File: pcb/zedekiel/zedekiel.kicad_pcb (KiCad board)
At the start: 2 copper layers, 150 parts, among them J2 USB_C_Receptacle_USB2.0, K1 KEYSW, K10 KEYSW, K11 KEYSW, K12 KEYSW, K13 KEYSW, K14 KEYSW, K15 KEYSW, K16 KEYSW, K17 KEYSW, K18 KEYSW, K19 KEYSW, K2 KEYSW, K20 KEYSW, K21 KEYSW, K22 KEYSW, K23 KEYSW, K24 KEYSW, K25 KEYSW, K26 KEYSW, K27 KEYSW, K28 KEYSW, K29 KEYSW, K3 KEYSW, K30 KEYSW, K31 KEYSW, K32 KEYSW, K33 KEYSW, K34 KEYSW, K35 KEYSW, K36 KEYSW, K37 KEYSW, K38 KEYSW, K39 KEYSW, K4 KEYSW, K40 KEYSW, K41 KEYSW, K42 KEYSW, K43 KEYSW, K44 KEYSW, K45 KEYSW, K46 KEYSW, K47 KEYSW, K48 KEYSW, K49 KEYSW, K5 KEYSW, K50 KEYSW, K51 KEYSW, K52 KEYSW, K53 KEYSW, K54 KEYSW, K55 KEYSW, K56 KEYSW, K57 KEYSW, K58 KEYSW, K59 KEYSW, K6 KEYSW, K60 KEYSW, K61 KEYSW, K62 KEYSW, K63 KEYSW, K64 KEYSW, K65 KEYSW, K66 KEYSW, K7 KEYSW, K8 KEYSW, K9 KEYSW, SW1 SW_PUSH, U1 ATmega16U4-AU_(modified), X1 16MHz

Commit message: Diodes and sockets in place
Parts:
- C1, C2, C3, C4, C5, C6, C7, C8, D1, D10, D11, D12, D13, D14, D15, D16, D17, D18, D19, D2, D20, D21, D22, D23, D24, D25, D26, D27, D28, D29, D3, D30, D31, D32, D33, D34, D35, D36, D37, D38, D39, D4, D40, D41, D42, D43, D44, D45, D46, D47, D48, D49, D5, D50, D51, D52, D53, D54, D55, D56, D57, D58, D59, D6, D60, D61, D62, D63, D64, D65, D66, D7, D8, D9, R1, R2, R3, R4, R5, R6, SW1, X1: moved to B.Cu
- moved D56 279.8 mm to (318.2, 92.8), turned to 270 degrees
- moved D55 246.5 mm to (285.0, 92.8), turned to 270 degrees
- moved D54 238.5 mm to (256.4, 92.8), turned to 270 degrees
- moved D42 236.8 mm to (313.4, 73.8), turned to 270 degrees
- moved D64 234.8 mm to (265.8, 111.8), turned to 270 degrees
- moved D63 234.0 mm to (235.0, 111.8), turned to 270 degrees
- moved D65 212.7 mm to (296.6, 111.8), turned to 270 degrees
- moved D41 206.5 mm to (285.0, 73.8), turned to 270 degrees
- moved D66 206.1 mm to (318.2, 35.8), turned to 270 degrees
- moved D62 205.4 mm to (211.2, 111.8), turned to 270 degrees
- moved D53 202.8 mm to (237.4, 92.8), turned to 270 degrees
- moved D61 185.3 mm to (187.4, 111.8), turned to 270 degrees
- moved D52 183.0 mm to (218.4, 92.8), turned to 270 degrees
- moved D40 171.7 mm to (266.0, 73.8), turned to 270 degrees
- moved D39 170.0 mm to (247.0, 73.8), turned to 270 degrees
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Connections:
- K1 pad 1: Net-(D1-Pad1) -> /R1
- K1 pad 2: /R1 -> Net-(D1-Pad1)
- K10 pad 1: Net-(D10-Pad1) -> /R1
- K10 pad 2: /R1 -> Net-(D10-Pad1)
- K11 pad 1: Net-(D11-Pad1) -> /R1
- K11 pad 2: /R1 -> Net-(D11-Pad1)
- K12 pad 1: Net-(D12-Pad1) -> /R1
- K12 pad 2: /R1 -> Net-(D12-Pad1)
- K13 pad 1: Net-(D13-Pad1) -> /R1
- K13 pad 2: /R1 -> Net-(D13-Pad1)
- K14 pad 1: Net-(D14-Pad1) -> /R1
- K14 pad 2: /R1 -> Net-(D14-Pad1)
- K15 pad 1: Net-(D15-Pad1) -> /R2
- K15 pad 2: /R2 -> Net-(D15-Pad1)
- K16 pad 1: Net-(D16-Pad1) -> /R2
- K16 pad 2: /R2 -> Net-(D16-Pad1)
- K17 pad 1: Net-(D17-Pad1) -> /R2
- K17 pad 2: /R2 -> Net-(D17-Pad1)
- K18 pad 1: Net-(D18-Pad1) -> /R2
- K18 pad 2: /R2 -> Net-(D18-Pad1)
- K19 pad 1: Net-(D19-Pad1) -> /R2
- K19 pad 2: /R2 -> Net-(D19-Pad1)
- K2 pad 1: Net-(D2-Pad1) -> /R1
- K2 pad 2: /R1 -> Net-(D2-Pad1)
- K20 pad 1: Net-(D20-Pad1) -> /R2
- K20 pad 2: /R2 -> Net-(D20-Pad1)
- K21 pad 1: Net-(D21-Pad1) -> /R2
- K21 pad 2: /R2 -> Net-(D21-Pad1)
- K22 pad 1: Net-(D22-Pad1) -> /R2
- K22 pad 2: /R2 -> Net-(D22-Pad1)
- K23 pad 1: Net-(D23-Pad1) -> /R2
- K23 pad 2: /R2 -> Net-(D23-Pad1)
- K24 pad 1: Net-(D24-Pad1) -> /R2
- K24 pad 2: /R2 -> Net-(D24-Pad1)
- K25 pad 1: Net-(D25-Pad1) -> /R2
- K25 pad 2: /R2 -> Net-(D25-Pad1)
- K26 pad 1: Net-(D26-Pad1) -> /R2
- K26 pad 2: /R2 -> Net-(D26-Pad1)
- K27 pad 1: Net-(D27-Pad1) -> /R2
- K27 pad 2: /R2 -> Net-(D27-Pad1)
- K28 pad 1: Net-(D28-Pad1) -> /R2
- K28 pad 2: /R2 -> Net-(D28-Pad1)
- K29 pad 1: Net-(D29-Pad1) -> /R3
- K29 pad 2: /R3 -> Net-(D29-Pad1)
- K3 pad 1: Net-(D3-Pad1) -> /R1
- K3 pad 2: /R1 -> Net-(D3-Pad1)
- K30 pad 1: Net-(D30-Pad1) -> /R3
- K30 pad 2: /R3 -> Net-(D30-Pad1)
- K31 pad 1: Net-(D31-Pad1) -> /R3
- K31 pad 2: /R3 -> Net-(D31-Pad1)
- K32 pad 1: Net-(D32-Pad1) -> /R3
- K32 pad 2: /R3 -> Net-(D32-Pad1)
- K33 pad 1: Net-(D33-Pad1) -> /R3
- K33 pad 2: /R3 -> Net-(D33-Pad1)
- K34 pad 1: Net-(D34-Pad1) -> /R3
- K34 pad 2: /R3 -> Net-(D34-Pad1)
- K35 pad 1: Net-(D35-Pad1) -> /R3
- K35 pad 2: /R3 -> Net-(D35-Pad1)
- K36 pad 1: Net-(D36-Pad1) -> /R3
- K36 pad 2: /R3 -> Net-(D36-Pad1)
- K37 pad 1: Net-(D37-Pad1) -> /R3
- K37 pad 2: /R3 -> Net-(D37-Pad1)
- K38 pad 1: Net-(D38-Pad1) -> /R3
- K38 pad 2: /R3 -> Net-(D38-Pad1)
- K39 pad 1: Net-(D39-Pad1) -> /R3
- K39 pad 2: /R3 -> Net-(D39-Pad1)
- K4 pad 1: Net-(D4-Pad1) -> /R1
- K4 pad 2: /R1 -> Net-(D4-Pad1)
- K40 pad 1: Net-(D40-Pad1) -> /R3
- K40 pad 2: /R3 -> Net-(D40-Pad1)
- K41 pad 1: Net-(D41-Pad1) -> /R3
- K41 pad 2: /R3 -> Net-(D41-Pad1)
- K42 pad 1: Net-(D42-Pad1) -> /R3
- K42 pad 2: /R3 -> Net-(D42-Pad1)
- K43 pad 1: Net-(D43-Pad1) -> /R4
- K43 pad 2: /R4 -> Net-(D43-Pad1)
- K44 pad 1: Net-(D44-Pad1) -> /R4
- K44 pad 2: /R4 -> Net-(D44-Pad1)
- K45 pad 1: Net-(D45-Pad1) -> /R4
- K45 pad 2: /R4 -> Net-(D45-Pad1)
- K46 pad 1: Net-(D46-Pad1) -> /R4
- K46 pad 2: /R4 -> Net-(D46-Pad1)
- K47 pad 1: Net-(D47-Pad1) -> /R4
- K47 pad 2: /R4 -> Net-(D47-Pad1)
- K48 pad 1: Net-(D48-Pad1) -> /R4
- K48 pad 2: /R4 -> Net-(D48-Pad1)
- K49 pad 1: Net-(D49-Pad1) -> /R4
- K49 pad 2: /R4 -> Net-(D49-Pad1)
- K5 pad 1: Net-(D5-Pad1) -> /R1
- K5 pad 2: /R1 -> Net-(D5-Pad1)
- K50 pad 1: Net-(D50-Pad1) -> /R4
- K50 pad 2: /R4 -> Net-(D50-Pad1)
- K51 pad 1: Net-(D51-Pad1) -> /R4
- K51 pad 2: /R4 -> Net-(D51-Pad1)
- K52 pad 1: Net-(D52-Pad1) -> /R4
- K52 pad 2: /R4 -> Net-(D52-Pad1)
- K53 pad 1: Net-(D53-Pad1) -> /R4
- K53 pad 2: /R4 -> Net-(D53-Pad1)
- K54 pad 1: Net-(D54-Pad1) -> /R4
- K54 pad 2: /R4 -> Net-(D54-Pad1)
- K55 pad 1: Net-(D55-Pad1) -> /R4
- K55 pad 2: /R4 -> Net-(D55-Pad1)
- K56 pad 1: Net-(D56-Pad1) -> /R4
- K56 pad 2: /R4 -> Net-(D56-Pad1)
- K57 pad 1: Net-(D57-Pad1) -> /R5
- K57 pad 2: /R5 -> Net-(D57-Pad1)
- K58 pad 1: Net-(D58-Pad1) -> /R5
- K58 pad 2: /R5 -> Net-(D58-Pad1)
- K59 pad 1: Net-(D59-Pad1) -> /R5
- K59 pad 2: /R5 -> Net-(D59-Pad1)
- K6 pad 1: Net-(D6-Pad1) -> /R1
- K6 pad 2: /R1 -> Net-(D6-Pad1)
- K60 pad 1: Net-(D60-Pad1) -> /R5
- K60 pad 2: /R5 -> Net-(D60-Pad1)
- K61 pad 1: Net-(D61-Pad1) -> /R5
- K61 pad 2: /R5 -> Net-(D61-Pad1)
- K62 pad 1: Net-(D62-Pad1) -> /R5
- K62 pad 2: /R5 -> Net-(D62-Pad1)
- K63 pad 1: Net-(D63-Pad1) -> /R5
- K63 pad 2: /R5 -> Net-(D63-Pad1)
- K64 pad 1: Net-(D64-Pad1) -> /R5
- K64 pad 2: /R5 -> Net-(D64-Pad1)
- K65 pad 1: Net-(D65-Pad1) -> /R5
- K65 pad 2: /R5 -> Net-(D65-Pad1)
- K66 pad 1: Net-(D66-Pad1) -> /R5
- K66 pad 2: /R5 -> Net-(D66-Pad1)
- K7 pad 1: Net-(D7-Pad1) -> /R1
- K7 pad 2: /R1 -> Net-(D7-Pad1)
- K8 pad 1: Net-(D8-Pad1) -> /R1
- K8 pad 2: /R1 -> Net-(D8-Pad1)
- K9 pad 1: Net-(D9-Pad1) -> /R1
- K9 pad 2: /R1 -> Net-(D9-Pad1)

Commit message: Holes and stabilizers
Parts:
- added REF**: Stabilizer_MX_2u, custom:Stabilizer_MX_2u, F.Cu at (39.4, 67.9)
- added REF**: Stabilizer_MX_2u, custom:Stabilizer_MX_2u, F.Cu at (303.0, 48.9)
- added REF**: Stabilizer_MX_2u, custom:Stabilizer_MX_2u, F.Cu at (305.4, 67.9)
- added REF**: Stabilizer_MX_2u, custom:Stabilizer_MX_2u, F.Cu at (276.9, 86.9)
- added REF**: Stabilizer_MX_2u, custom:Stabilizer_MX_2u, F.Cu at (257.9, 105.9)
- added REF**: Stabilizer_MX_2u, custom:Stabilizer_MX_2u, F.Cu at (146.3, 105.9)
- added REF**: Stabilizer_MX_2u, custom:Stabilizer_MX_2u, F.Cu at (63.1, 105.9)
- J2, U1: moved to B.Cu
- SW1: moved to F.Cu
- moved R1 235.3 mm to (-24.9, 96.0), turned to 270 degrees
- moved C5 233.5 mm to (-2.05, 80.5)
- moved C6 219.7 mm to (-2.05, 76.4)
- moved C2 219.3 mm to (26.9, 109.1), turned to 180 degrees
- moved R4 218.0 mm to (27.6, 97.7)
- moved R6 213.4 mm to (42.5, 112.9)
- moved C1 211.3 mm to (24.1, 100.9)
- moved C7 201.2 mm to (-2.12, 84.1)
- moved C4 201.1 mm to (-2.15, 72.3)
- moved R5 197.6 mm to (24.4, 97.8)
- moved C8 196.4 mm to (-2.15, 68.3)
- moved C3 192.8 mm to (23.6, 109.1)
- moved R2 190.5 mm to (-7.70, 17.0), turned to 180 degrees
- moved R3 186.2 mm to (-7.54, 12.8), turned to 180 degrees
- moved SW1 125.9 mm to (-26.4, 101.2)
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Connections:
- D57 pad 2: /C1 -> /C2
- D58 pad 2: /C2 -> /C4
- D59 pad 2: /C3 -> /C5
- D60 pad 2: /C4 -> /C7
- D61 pad 2: /C5 -> /C8
- D62 pad 2: /C6 -> /C10
- D63 pad 2: /C7 -> /C11
- D64 pad 2: /C8 -> /C12
- D65 pad 2: /C9 -> /C13
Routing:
- net Net-(D7-Pad1): track 0.00 -> 7.34 mm
- net Net-(D55-Pad1): track 0.00 -> 2.53 mm
- net Net-(D41-Pad1): track 0.00 -> 2.53 mm
- net Net-(D40-Pad1): track 0.00 -> 2.53 mm
- net Net-(D32-Pad1): track 0.00 -> 2.53 mm
- net Net-(D31-Pad1): track 0.00 -> 2.53 mm
- net Net-(D30-Pad1): track 0.00 -> 2.53 mm
- net Net-(D39-Pad1): track 0.00 -> 2.53 mm
- net Net-(D38-Pad1): track 0.00 -> 2.53 mm
- net Net-(D37-Pad1): track 0.00 -> 2.53 mm
- net Net-(D36-Pad1): track 0.00 -> 2.53 mm
- net Net-(D35-Pad1): track 0.00 -> 2.53 mm
- net Net-(D34-Pad1): track 0.00 -> 2.53 mm
- net Net-(D33-Pad1): track 0.00 -> 2.53 mm
- net Net-(D57-Pad1): track 0.00 -> 2.51 mm
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
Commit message: Routing started.
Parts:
- added REF**: hole-indicator, custom:hole-indicator, F.Cu at (297.0, 95.0)
- added REF**: hole-indicator, custom:hole-indicator, F.Cu at (166.4, 105.9)
- added REF**: hole-indicator, custom:hole-indicator, F.Cu at (47.4, 88.8)
- added REF**: hole-indicator, custom:hole-indicator, F.Cu at (248.4, 65.5)
- added REF**: hole-indicator, custom:hole-indicator, F.Cu at (115.4, 65.5)
- added REF**: hole-indicator, custom:hole-indicator, F.Cu at (46.0, 39.4)
- added REF**: hole-indicator, custom:hole-indicator, F.Cu at (298.9, 35.4)
- added REF**: hole-indicator, custom:hole-indicator, F.Cu at (162.9, 38.8)
- moved J2 87.5 mm to (-23.5, 62.6)
- moved R2 87.5 mm to (-77.8, 69.4)
- moved R3 87.5 mm to (-77.6, 65.2)
- moved R5 76.6 mm to (46.0, 24.3), turned to 90 degrees
- moved R4 75.0 mm to (43.1, 24.3), turned to 90 degrees
- moved C5 56.4 mm to (46.4, 109.3), turned to 225 degrees
- moved SW1 50.2 mm to (22.9, 92.0), turned to 270 degrees
- moved R1 47.8 mm to (22.9, 97.9), turned to 90 degrees
- moved C7 47.3 mm to (43.5, 96.5), turned to 315 degrees
- moved C4 42.2 mm to (30.6, 98.9), turned to 45 degrees
- moved C8 41.2 mm to (22.9, 101.0), turned to 270 degrees
- moved C6 40.5 mm to (33.1, 96.4), turned to 45 degrees
- moved R6 12.6 mm to (29.9, 112.9), turned to 180 degrees
- moved C1 6.43 mm to (23.6, 107.3)
- moved C2 0.20 mm to (26.9, 108.9)
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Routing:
- net /R5: track 0.00 -> 336.1 mm, vias 0 -> 10
- net /R4: track 0.00 -> 286.7 mm, vias 0 -> 14
- net /R3: track 0.00 -> 277.2 mm, vias 0 -> 14
- net /R2: track 0.00 -> 276.5 mm, vias 0 -> 14
- net /R1: track 0.00 -> 259.8 mm, vias 0 -> 14
- net /C12: track 0.00 -> 95.1 mm
- net /C7: track 0.00 -> 93.0 mm
- net /C13: track 0.00 -> 92.3 mm
- net /C2: track 0.00 -> 91.2 mm
- net /C8: track 0.00 -> 91.0 mm
- net /C14: track 0.00 -> 89.9 mm
- net /C10: track 0.00 -> 89.7 mm
- net /C5: track 0.00 -> 87.9 mm
- net /C11: track 0.00 -> 87.9 mm
- net /C4: track 0.00 -> 87.7 mm
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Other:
- net class EasyEDA added: clearance 0.2, trace_width 0.254, via_dia 0.61, via_drill 0.305
- board text added: "RESET"

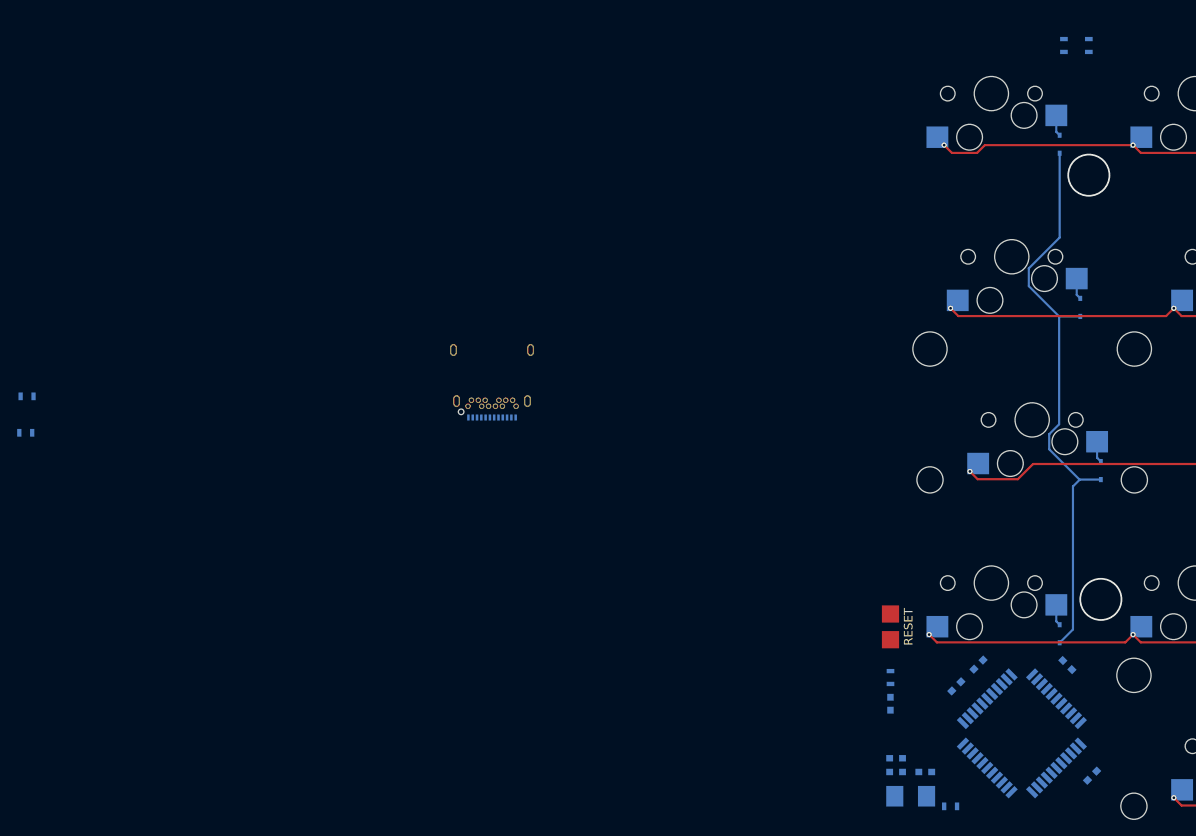
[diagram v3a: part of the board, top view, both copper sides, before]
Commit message: Routing. Fixed a moved socket.
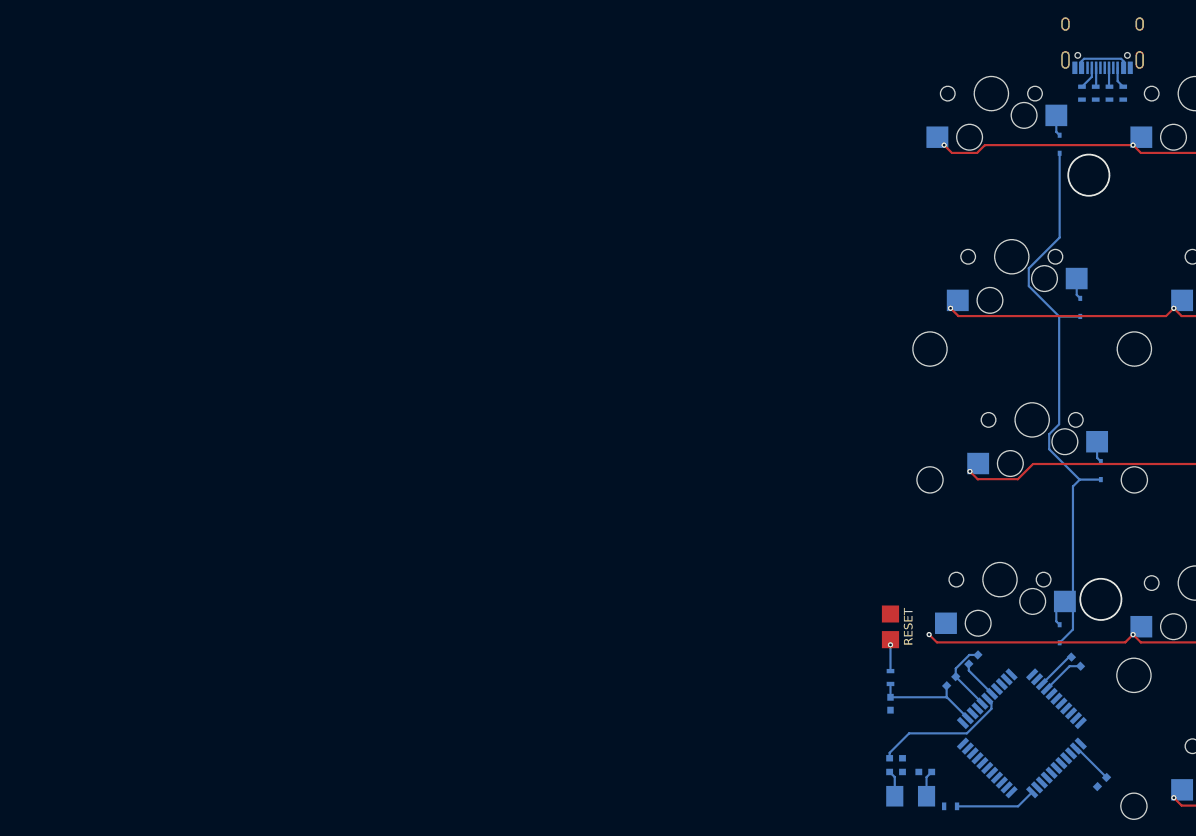
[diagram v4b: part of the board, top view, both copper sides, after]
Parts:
- removed J2: USB_C_Receptacle_USB2.0, Connectors_USB:USB_C_Receptacle_Amphenol_12401548E4-2A
- added USB1: HRO-TYPE-C, Type-C:HRO-TYPE-C-31-M-12, B.Cu at (47.6, 19.2)
- moved R3 132.4 mm to (50.0, 29.9), turned to 270 degrees
- moved R2 129.2 mm to (45.2, 29.9), turned to 270 degrees
- moved R4 7.67 mm to (48.4, 29.9)
- moved R5 5.61 mm to (46.8, 29.9)
- moved C5 1.38 mm to (47.5, 110.1)
- moved C7 1.08 mm to (44.5, 96.0)
- moved K43 1.08 mm to (35.6, 86.5)
- moved C6 0.85 mm to (32.5, 95.8)
- moved C4 0.85 mm to (30.0, 98.3)
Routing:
- net VCC: track 0.00 -> 33.9 mm
- net Net-(C1-Pad1): track 0.00 -> 16.0 mm
- net GND: track 0.00 -> 13.6 mm
- net Net-(R6-Pad1): track 0.00 -> 9.43 mm
- net Net-(C3-Pad1): track 0.00 -> 3.07 mm
- net Net-(C2-Pad1): track 0.00 -> 3.07 mm
- net Net-(R1-Pad2): track 0.00 -> 3.05 mm, vias 0 -> 1
- net Net-(R2-Pad1): track 0.00 -> 2.68 mm
- net Net-(R3-Pad1): track 0.00 -> 2.47 mm
- net Net-(R5-Pad2): track 0.00 -> 2.23 mm
- net Net-(R4-Pad2): track 0.00 -> 2.23 mm
